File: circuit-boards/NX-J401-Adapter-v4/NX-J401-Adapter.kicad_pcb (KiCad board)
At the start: 4 copper layers, 100 x 79 mm, 35 parts, among them J1 18V_OUT, J2 NX-BUTTON, J3 CONSOLE, J4 Power, Q1 CSD16322Q5, Q2 SI4483ADY-T1-GE3, SW1 RESET, SW2 RECOVERY, U1 LM3478MA

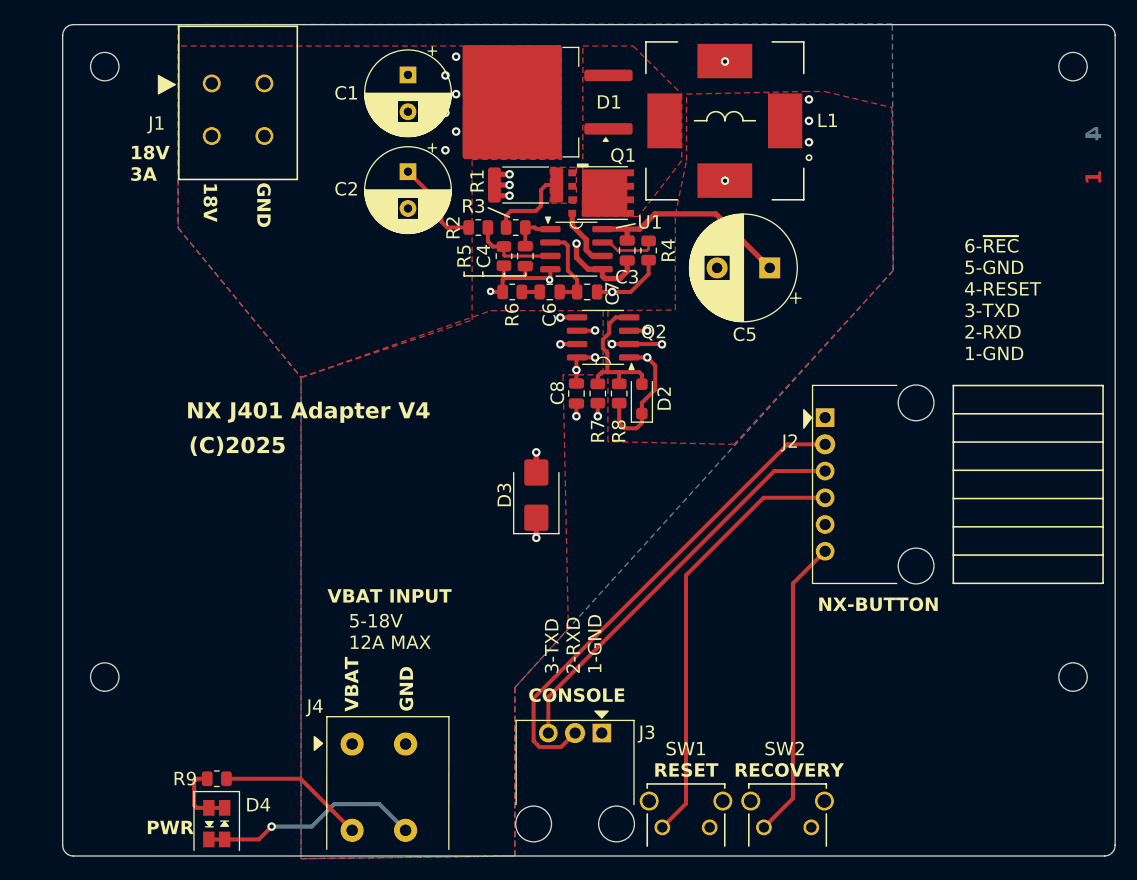
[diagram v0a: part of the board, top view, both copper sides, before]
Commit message: Update NX J401 Adapter to add PC LED and swap buttons
Signed-off-by: Scott Berman <sgberman1@gmail.com>
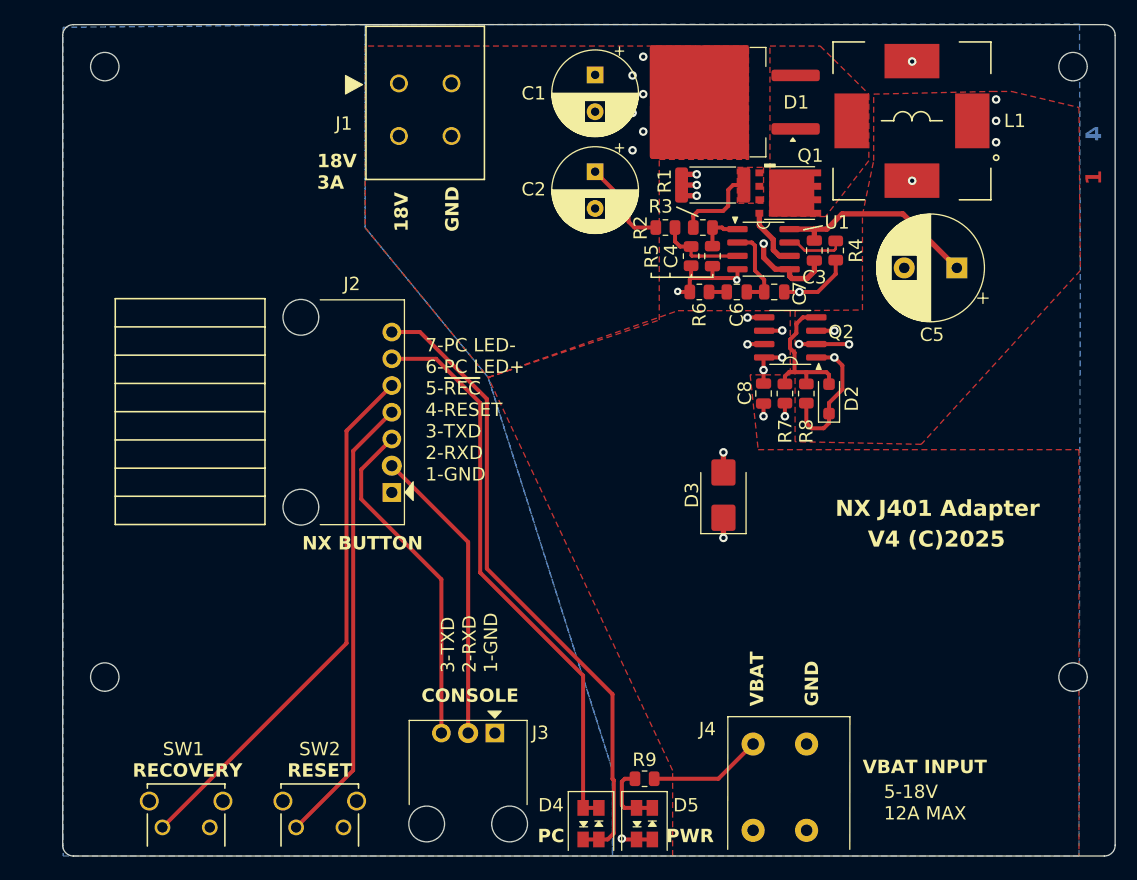
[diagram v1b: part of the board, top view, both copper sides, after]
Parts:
- added D4: PC, NX-J401-Adapter:LED-Dialight-5913001858F, F.Cu at (275.2, 155.9)
- J2: value NX-BUTTON -> NX BUTTON; footprint NX-J401-Adapter:70555-0005 -> NX-J401-Adapter:70555-0006
- moved SW1 57.1 mm to (234.5, 156.3)
- moved J2 41.3 mm to (256.3, 116.8), turned to 180 degrees
- moved D5 40.6 mm to (280.3, 155.9)
- moved R9 40.6 mm to (280.3, 151.7)
- moved J4 38.1 mm to (290.6, 148.4)
- moved SW2 34.8 mm to (247.2, 156.3)
- moved C3 17.8 mm to (296.4, 101.5)
- moved C5 17.8 mm to (310.0, 103.1)
- moved C6 17.8 mm to (289.1, 105.4)
- moved C7 17.8 mm to (292.6, 105.4)
- moved D1 17.8 mm to (287.0, 87.4)
- moved Q2 17.8 mm to (294.1, 109.7)
- moved R1 17.8 mm to (286.8, 95.2)
- moved R3 17.8 mm to (285.8, 99.3)
- moved R7 17.8 mm to (293.6, 115.1)
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- renumbered D4 to D5, SW2 to SW1, SW1 to SW2
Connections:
- J2 pad 5: /RTN -> /~{REC}
- J2 pad 6: /~{REC} -> Net-(D4A-Red-K)
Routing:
- net Net-(D4A-RedA): track 0.00 -> 61.1 mm
- net Net-(D4A-Red-K): track 0.00 -> 54.2 mm
- net /~{REC}: track 28.6 -> 51.0 mm
- net GND: track 57.7 -> 39.5 mm
- net /UART2_RXD: track 46.5 -> 28.4 mm
- net /UART2_TXD: track 38.6 -> 32.3 mm
- net /V_BAT: track 25.0 -> 21.8 mm
- net /~{SYS_RESET}: track 41.2 -> 43.2 mm
- added copper zone on B.Cu, net /RTN
- removed copper zone on In1.Cu, net GND
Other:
- board text added: "7-PC LED- 6-PC LED+ 5-~{REC} 4-RESET 3-TXD 2-RXD 1-GND"
- board text added: "NX J401 Adapter"
- board text added: "V4 (C)2025"
- board text removed: "(C)2025"
- board text removed: "6-~{REC} 5-GND 4-RESET 3-TXD 2-RXD 1-GND"
- board text removed: "NX J401 Adapter V4"

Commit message: Update NX-J401 and NX Button Interface boards
Signed-off-by: Scott Berman <scott.berman@bluerivertech.com>
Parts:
- moved D3 25.2 mm to (303.4, 144.5)
- moved J1 2.39 mm to (256.9, 88.0)
- moved D4 0.63 mm to (274.6, 155.9)
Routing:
- net /Power Supply/V_IN: track 39.4 -> 27.9 mm, vias 7 -> 0
- net /V_BAT: track 21.8 -> 13.3 mm, vias 6 -> 0
- net Net-(D4A-RedA): track 61.1 -> 58.9 mm
- net Net-(D4A-Red-K): track 54.2 -> 52.5 mm
- net /UART2_RXD: track 28.4 -> 29.4 mm
- net /+18V_OUT: vias 6 -> 0
- removed copper zone on In1.Cu, net /+18V_OUT
- removed copper zone on In1.Cu, net /Power Supply/V_IN
- removed copper zone on In1.Cu, net /RTN
- removed copper zone on In2.Cu, net /RTN
- removed copper zone on In1.Cu, net /V_BAT
- removed copper zone on In2.Cu, net GND
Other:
- copper layers 4 -> 2
- board text added: "0.02"
- board text added: "1. Layers: 2 2. PCB Thickness: 1.6 mm 3. PCB Color: GREEN 4. Material Type: FR-4 TG155 5. Surface Finish: HASL 6. Outer Copper Weight: 1 oz 7. Impedance Control: NO 8. Layer Stackup: xxxx 9. Via Covering: Plugged 10. Min Via Hole Size / Diameter: 0.406 mm / 0.81 mm 11. Board Outline Tolerance: +/- 0.2 mm 12. Silk Screen: INK-JET/SCREEN PRINTING 13. Stencil Framwork: YES 14. Sencil Polishing: Elec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"
- board text added: "16.00 mils"
- board text added: "4.5"
- board text added: "59.12913 mils"
- board text added: "FR4"
- board text removed: "0.6 mils"
- board text removed: "1. Layers: 4 2. PCB Thickness: 1.6 mm 3. PCB Color: GREEN 4. Material Type: FR-4 TG155 5. Surface Finish: HASL 6. Outer Copper Weight: 1 oz 7. Inner Copper Weight: 0.5 oz 8. Impedance Control: NO 9. Layer Stackup: xxxx 10. Via Covering: Plugged 11. Min Via Hole Size / Diameter: 0.406 mm / 0.81 mm 12. Board Outline Tolerance: +/- 0.2 mm 13. Silk Screen: INK-JET/SCREEN PRINTING 14. Stencil Framwork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"
- board text removed: "11.81 mils"
- board text removed: "3"
- board text removed: "4"
- board text removed: "41.92913 mils"
- board text removed: "8 mils"
- board text removed: "Dielectric 2"
- board text removed: "Dielectric 3"
- board text removed: "In1.Cu"
- board text removed: "In2.Cu"
- board text removed: "prepreg"

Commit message: Minor fixes
Signed-off-by: Scott Berman <scott.berman@bluerivertech.com>
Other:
- board text added: "ORIN J401 Adapter V4 1868 SPACE COOKIES 4646 WILDCARD ROBOTICS (C)2025"
- board text removed: "NX J401 Adapter"
- board text removed: "V4 (C)2025"
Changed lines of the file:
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@@
 		(tags "resistor")
 		(property "Reference" "R2"
-			(at 2.3622 -0.0254 90)
+			(at 2.4892 -0.0254 90)
 			(layer "F.SilkS")
 			(effects
@@
 		(tags "SOIC SO")
 		(property "Reference" "Q2"
-			(at -4.826 0.508 180)
+			(at -4.9276 0 180)
 			(layer "F.SilkS")
 			(effects
@@
 		(tags "resistor")
 		(property "Reference" "R3"
-			(at -4.0151 -2.0066 0)
+			(at -4.0659 -2.0066 0)
 			(layer "F.SilkS")
 			(effects
@@
 		(tags "capacitor")
 		(property "Reference" "C7"
-			(at 2.413 0.127 90)
+			(at 2.54 0.2032 90)
 			(layer "F.SilkS")
 			(effects
@@
 		)
 	)
-	(gr_text "NX J401 Adapter"
-		(at 298.413715 126.873 0)
+	(gr_text "ORIN J401 Adapter V4\n\n1868 SPACE COOKIES\n4646 WILDCARD ROBOTICS\n(C)2025"
+		(at 287.782 135.2042 0)
 		(layer "F.SilkS")
 		(effects
@@
 		)
 	)
-	(gr_text "V4 (C)2025"
-		(at 301.498 129.794 0)
-		(layer "F.SilkS")
-		(effects
-			(font
-				(size 1.524 1.524)
-				(thickness 0.3048)
-				(bold yes)
-			)
-			(justify left bottom)
-		)
-	)
 	(gr_text "VBAT"
 		(at 291.719 144.78 90)
@@
 	)
 	(segment
-		(start 294.067 101.981)
-		(end 293.092001 101.981)
+		(start 291.195 99.110009)
+		(end 291.195 97.932)
 		(width 0.508)
 		(layer "F.Cu")
@@
 	)
 	(segment
-		(start 292.520222 101.409221)
-		(end 292.520222 100.435231)
+		(start 294.067 101.981)
+		(end 292.735 101.981)
 		(width 0.508)
 		(layer "F.Cu")
@@
 	)
 	(segment
-		(start 291.195 99.110009)
-		(end 291.195 97.932)
+		(start 292.520222 101.766222)
+		(end 292.520222 100.435231)
 		(width 0.508)
 		(layer "F.Cu")
@@
 	)
 	(segment
-		(start 293.092001 101.981)
-		(end 292.520222 101.409221)
+		(start 292.735 101.981)
+		(end 292.520222 101.766222)
 		(width 0.508)
 		(layer "F.Cu")
@@
 	)
 	(segment
-		(start 284.7086 101.0939)
-		(end 284.7086 101.9302)
-		(width 0.3048)
-		(layer "F.Cu")
-		(net 16)
-	)
-	(segment
-		(start 284.7784 102)
-		(end 285.491298 102)
-		(width 0.3048)
-		(layer "F.Cu")
-		(net 16)
-	)
-	(segment
 		(start 283.1827 99.2886)
 		(end 283.1827 100.6075)
@@
 	)
 	(segment
-		(start 284.7086 101.9302)
-		(end 284.7784 102)
+		(start 284.8375 101.0939)
+		(end 285.7436 102)
 		(width 0.3048)
 		(layer "F.Cu")
@@
 	)
 	(segment
-		(start 285.491298 102)
-		(end 285.492198 102.0009)
+		(start 284.7086 101.0939)
+		(end 284.8375 101.0939)
 		(width 0.3048)
 		(layer "F.Cu")
@@
 	)
 	(segment
-		(start 289.0971 102.0009)
-		(end 289.117 101.981)
+		(start 285.7436 102)
+		(end 289.098 102)
 		(width 0.3048)
 		(layer "F.Cu")
@@
 	)
 	(segment
-		(start 285.492198 102.0009)
-		(end 289.0971 102.0009)
+		(start 289.098 102)
+		(end 289.117 101.981)
 		(width 0.3048)
 		(layer "F.Cu")
@@
 	)
 	(segment
-		(start 298.45 101.3206)
+		(start 298.32106 100.56054)
 		(end 298.45 100.56054)
-		(width 0.254)
+		(width 0.3048)
 		(layer "F.Cu")
 		(net 17)
 	)
 	(segment
-		(start 294.7416 100.711)
-		(end 295.5036 101.473)
-		(width 0.254)
+		(start 295.59884 101.46664)
+		(end 297.41496 101.46664)
+		(width 0.3048)
 		(layer "F.Cu")
 		(net 17)
@@
 	(segment
 		(start 294.067 100.711)
-		(end 294.7416 100.711)
-		(width 0.254)
+		(end 294.8432 100.711)
+		(width 0.3048)
 		(layer "F.Cu")
 		(net 17)
 	)
 	(segment
-		(start 298.2976 101.473)
-		(end 298.45 101.3206)
-		(width 0.254)
+		(start 294.8432 100.711)
+		(end 295.59884 101.46664)
+		(width 0.3048)
 		(layer "F.Cu")
 		(net 17)
 	)
 	(segment
-		(start 295.5036 101.473)
-		(end 298.2976 101.473)
-		(width 0.254)
+		(start 297.41496 101.46664)
+		(end 298.32106 100.56054)
+		(width 0.3048)
 		(layer "F.Cu")
 		(net 17)
